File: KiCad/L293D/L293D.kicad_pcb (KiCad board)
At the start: 2 copper layers, 41.3 x 45.1 mm, 15 parts, among them J1 Conn_01x02_Socket, J10 Conn_01x03_Pin, J11 Conn_01x03_Pin, J12 Conn_01x02_Socket, J5 Conn_01x02_Pin, J6 Conn_01x02_Pin, J7 Conn_01x02_Pin, J8 Conn_01x02_Pin, J9 Conn_01x02_Socket, SW1 SW_SPDT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

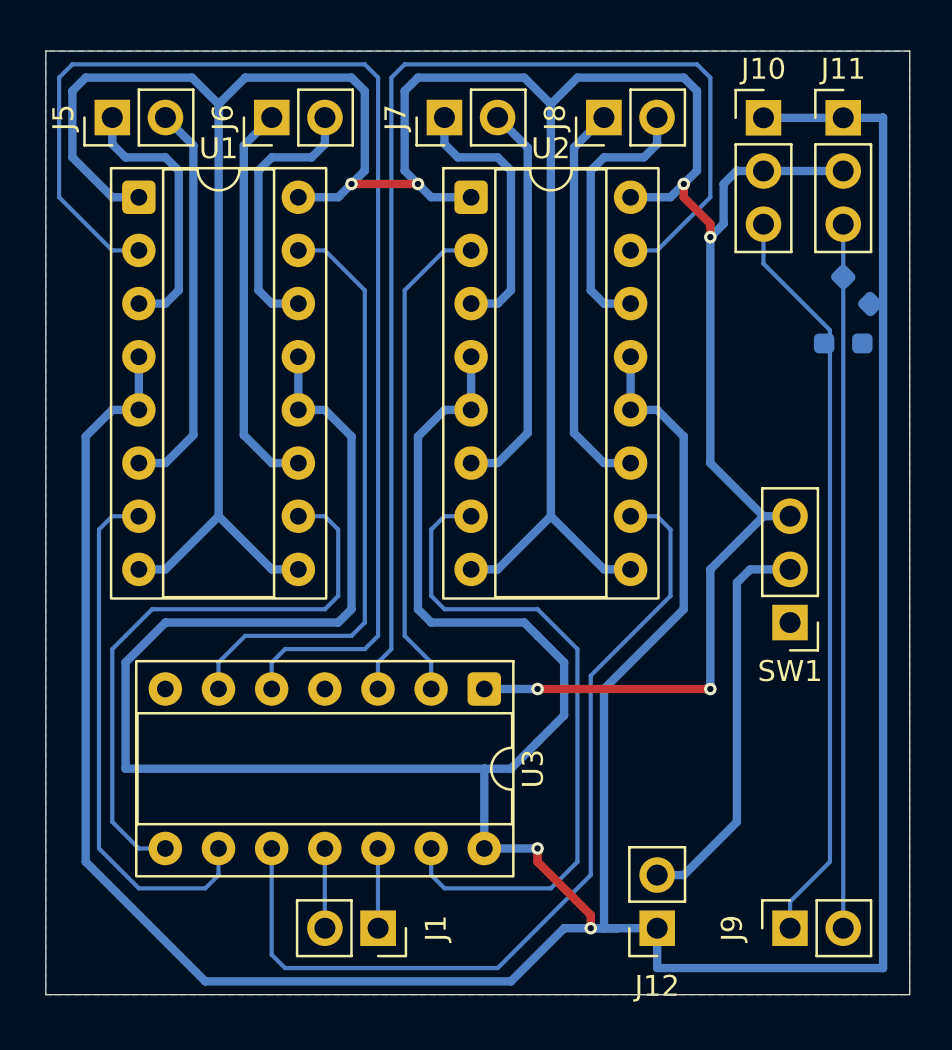
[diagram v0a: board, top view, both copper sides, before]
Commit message: ビアをでかくした
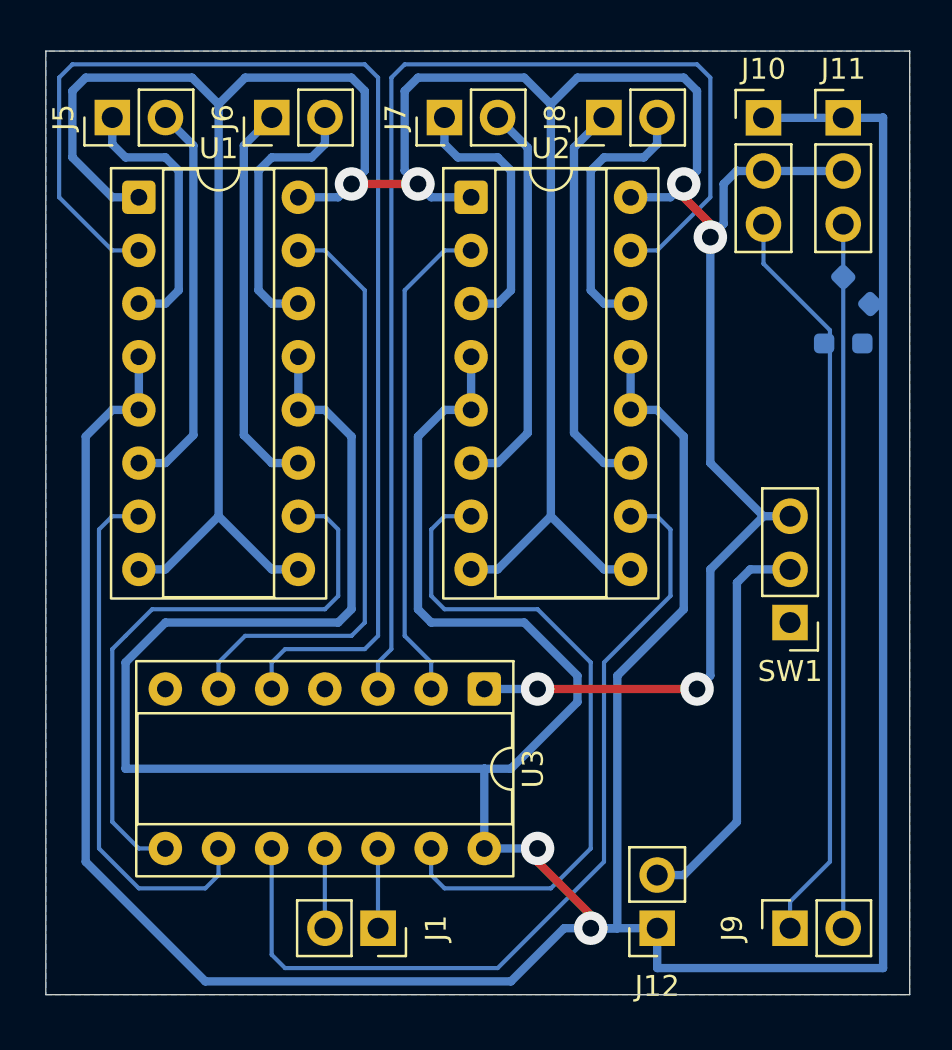
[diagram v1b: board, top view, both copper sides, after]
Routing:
- net /Motor3_B_In: track 32.6 -> 33.1 mm

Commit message: L293D基板を更新 出力に直列抵抗を追加 パスコンを追加 リセット入力を追加
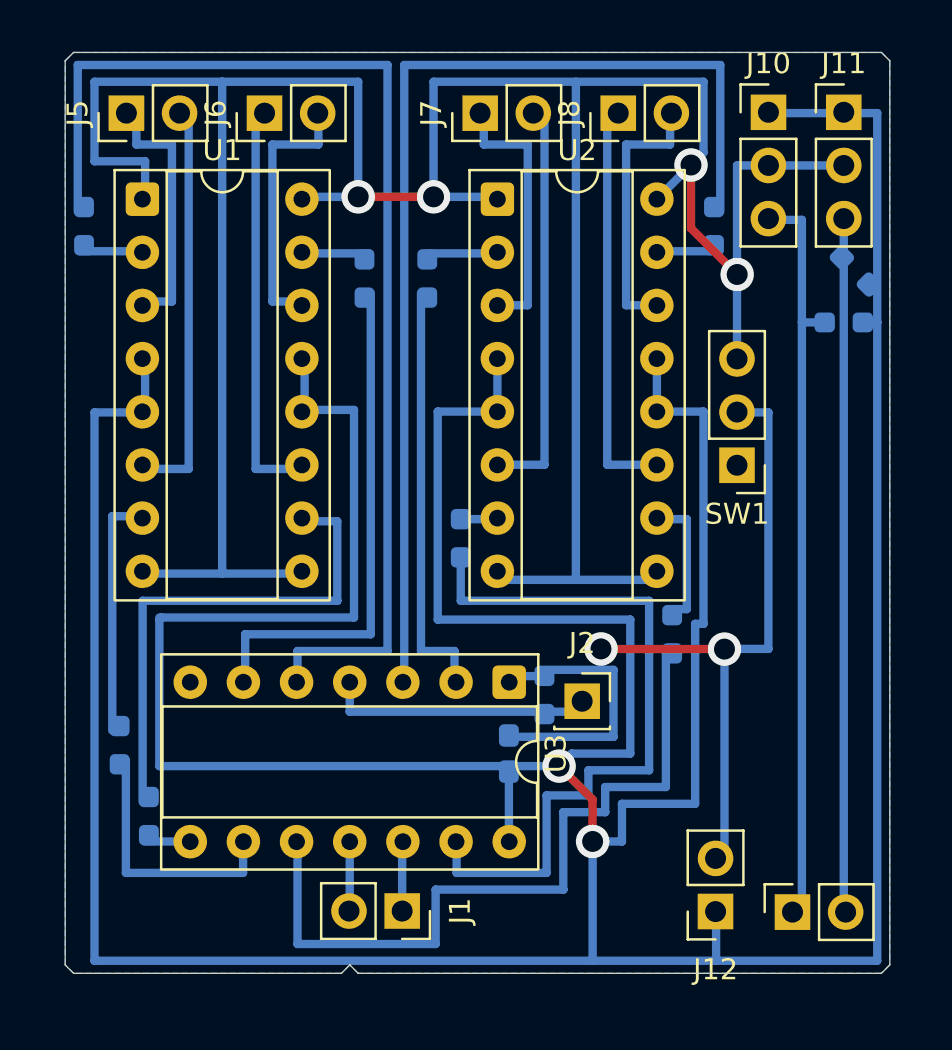
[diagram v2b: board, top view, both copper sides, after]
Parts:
- added C1: C, Capacitor_SMD:C_0603_1608Metric_Pad1.08x0.95mm_HandSolder, B.Cu at (101.5, 123.1)
- added J2: Conn_01x01_Socket, Connector_PinSocket_2.54mm:PinSocket_1x01_P2.54mm_Vertical, F.Cu at (105.0, 120.6)
- added R10: R, Resistor_SMD:R_0603_1608Metric_Pad0.98x0.95mm_HandSolder, B.Cu at (111.3, 97.9)
- added R11: R, Resistor_SMD:R_0603_1608Metric_Pad0.98x0.95mm_HandSolder, B.Cu at (103.2, 120.3)
- added R3: R, Resistor_SMD:R_0603_1608Metric_Pad0.98x0.95mm_HandSolder, B.Cu at (81.2, 97.9)
- added R4: R, Resistor_SMD:R_0603_1608Metric_Pad0.98x0.95mm_HandSolder, B.Cu at (82.9, 122.7)
- added R5: R, Resistor_SMD:R_0603_1608Metric_Pad0.98x0.95mm_HandSolder, B.Cu at (84.3, 126.1)
- added R6: R, Resistor_SMD:R_0603_1608Metric_Pad0.98x0.95mm_HandSolder, B.Cu at (94.6, 100.4)
- added R7: R, Resistor_SMD:R_0603_1608Metric_Pad0.98x0.95mm_HandSolder, B.Cu at (97.6, 100.4)
- added R8: R, Resistor_SMD:R_0603_1608Metric_Pad0.98x0.95mm_HandSolder, B.Cu at (99.2, 112.8)
- added R9: R, Resistor_SMD:R_0603_1608Metric_Pad0.98x0.95mm_HandSolder, B.Cu at (109.3, 117.4)
- moved SW1 7.93 mm to (112.4, 109.3)
- moved J12 2.90 mm to (111.4, 130.7)
- moved J7 1.72 mm to (100.1, 92.5)
- moved J1 1.41 mm to (96.4, 130.6)
- moved U2 1.26 mm to (101.0, 96.6)
- moved U3 1.23 mm to (101.5, 119.7)
- moved R1 1.01 mm to (117.5, 102.5)
- moved R2 0.93 mm to (118.1, 100.0)
- moved J9 0.78 mm to (115.0, 130.7)
- moved J8 0.72 mm to (106.7, 92.5)
- moved J5 0.71 mm to (83.2, 92.5)
- moved J6 0.40 mm to (89.8, 92.5)
- moved J10 0.35 mm to (113.9, 92.5)
- moved J11 0.27 mm to (117.5, 92.5)
- moved U1 0.19 mm to (84.0, 96.6)
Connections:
- J12 pad 2: /VCC -> VCC
- SW1 pad 2: /VCC -> VCC
- U1 pad 10: /Motor2_B_In -> Net-(U1-3A)
- U1 pad 15: /Motor2_A_In -> Net-(U1-4A)
- U1 pad 2: /Motor1_A_In -> Net-(U1-1A)
- U1 pad 7: /Motor1_B_In -> Net-(U1-2A)
- U2 pad 10: /Motor4_B_In -> Net-(U2-3A)
- U2 pad 15: /Motor4_A_In -> Net-(U2-4A)
- U2 pad 2: /Motor3_A_In -> Net-(U2-1A)
- U2 pad 7: /Motor3_B_In -> Net-(U2-2A)
- U3 pad 1: +5V -> VCC
- U3 pad 4: unconnected-(U3-~{RESET}/PB3-Pad4) -> Net-(J2-Pin_1)
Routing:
- net VCC: track 0.00 -> 42.4 mm, vias 0 -> 2
- net +5V: track 170.0 -> 142.2 mm, vias 6 -> 4
- net /Motor2_B_In: track 28.5 -> 1.50 mm
- net Net-(U1-3A): track 0.00 -> 24.5 mm
- net /VCC: track 19.1 -> 0.00 mm
- net /Motor1_B_In: track 25.4 -> 11.9 mm
- net Net-(J2-Pin_1): track 0.00 -> 12.4 mm
- net Net-(U1-2A): track 0.00 -> 11.8 mm
- net GND: track 236.4 -> 244.1 mm
- net Net-(U2-3A): track 0.00 -> 6.65 mm
- net /Motor4_B_In: track 42.7 -> 36.6 mm
- net /Motor2_A_In: track 28.9 -> 24.5 mm
- net /Motor1_A_In: track 59.9 -> 55.6 mm
- net /Motor4_A_In: track 55.8 -> 51.5 mm
- net /Motor3_A_In: track 23.5 -> 20.0 mm
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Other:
- board size 41.3 x 45.1 mm -> 39.4 x 44 mm
